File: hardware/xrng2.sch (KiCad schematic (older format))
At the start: 33 parts, among them J101 AVR-PDI-6A, J102 GS3, J103 GS3, J104 Conn_01x02, J105 Conn_01x03, J106 Conn_01x02, J107 USB_B, U101 CD4007, U102 XMEGA64A3U-A, U103 CD4007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

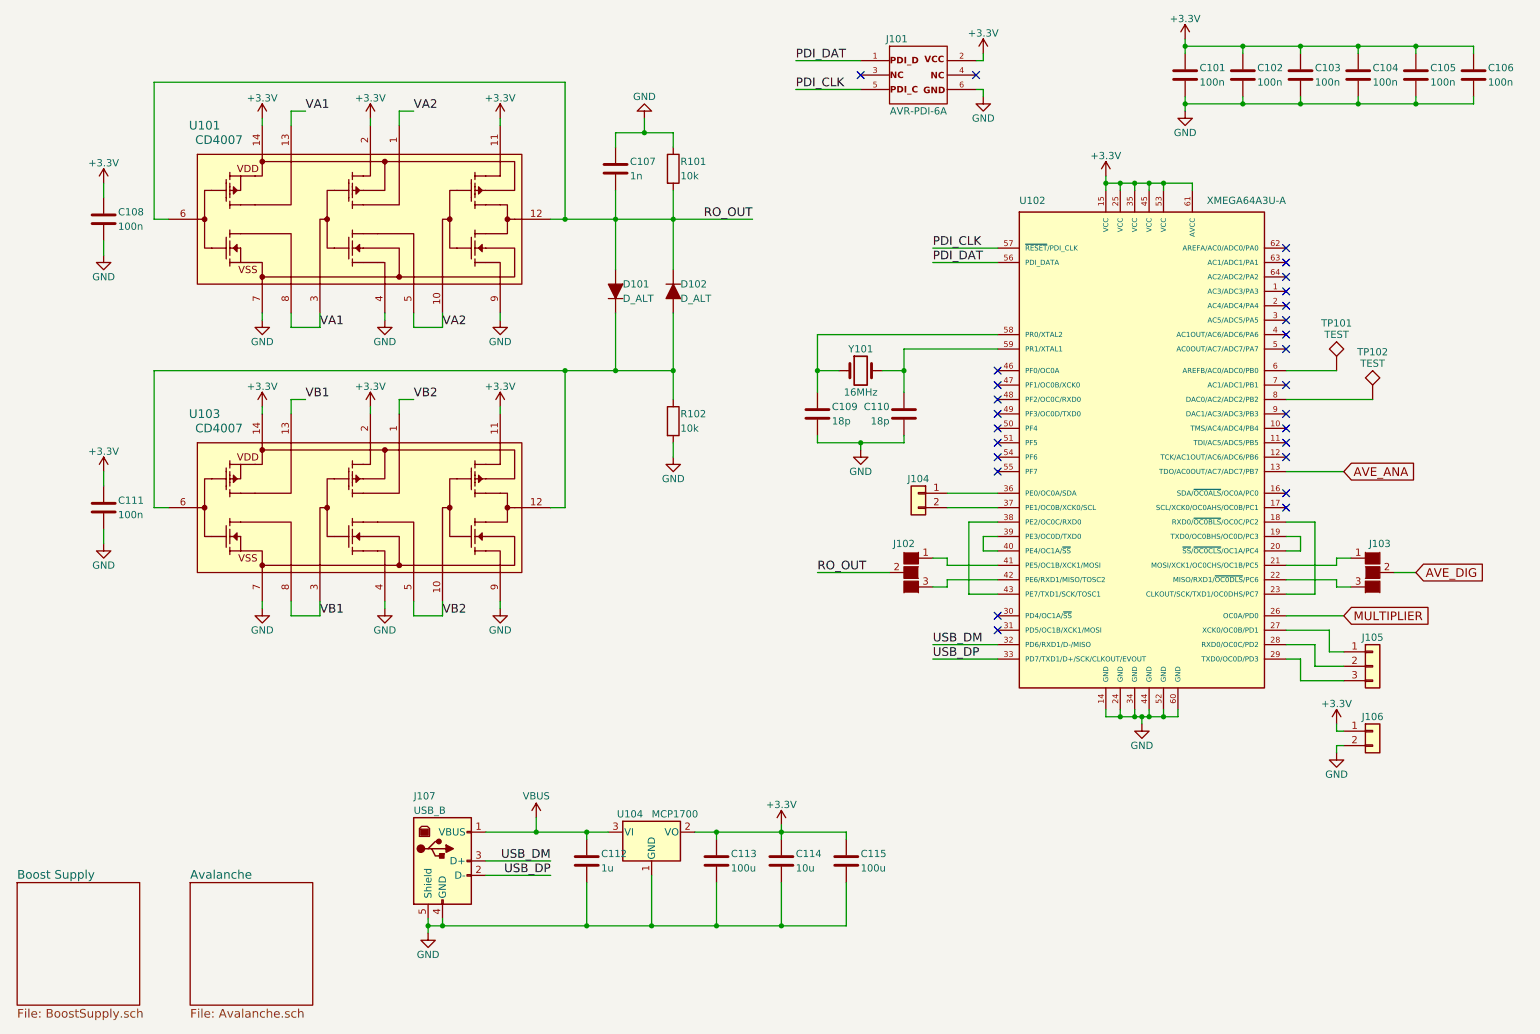
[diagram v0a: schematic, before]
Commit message: Pull-ups for I2C
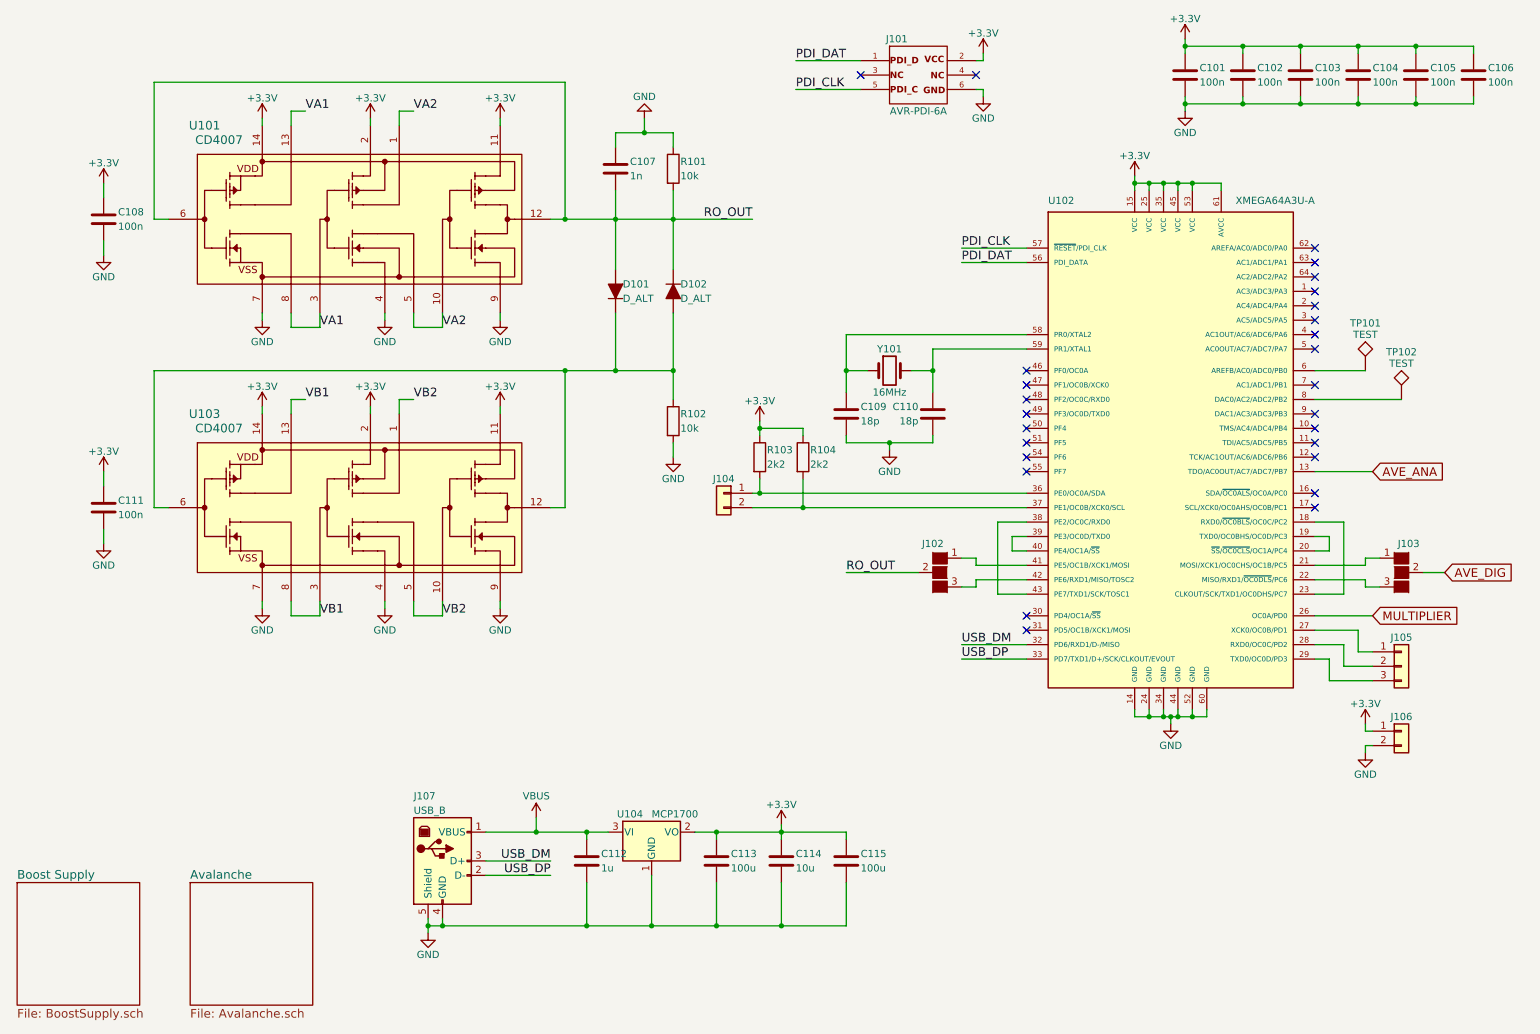
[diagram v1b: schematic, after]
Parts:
- added R103, R104: 2k2, Resistors_SMD:R_0603_HandSoldering, symbol R
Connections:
- net +3V3: now also R103.1, R104.1
- net at J104.1 (Pin_1), U102.36 (PE0/OC0A/SDA): now also R103.2
- net at J104.2 (Pin_2), U102.37 (PE1/OC0B/XCK0/SCL): now also R104.2
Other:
- moved on the sheet: C109, C110, J102, J103, J104, J105, J106, TP101, TP102, U102, Y101

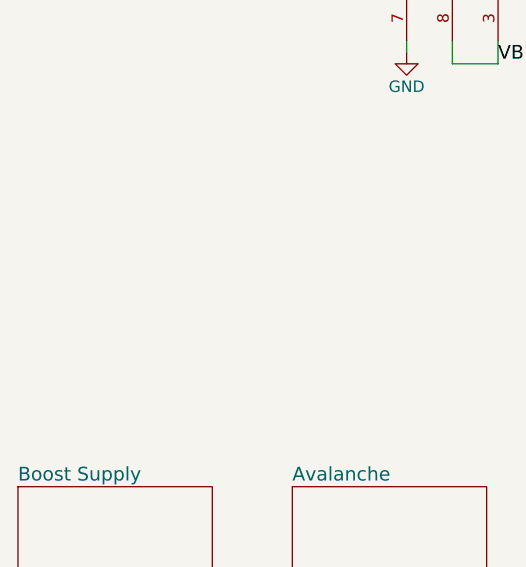
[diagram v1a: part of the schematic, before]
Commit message: Mounting holes
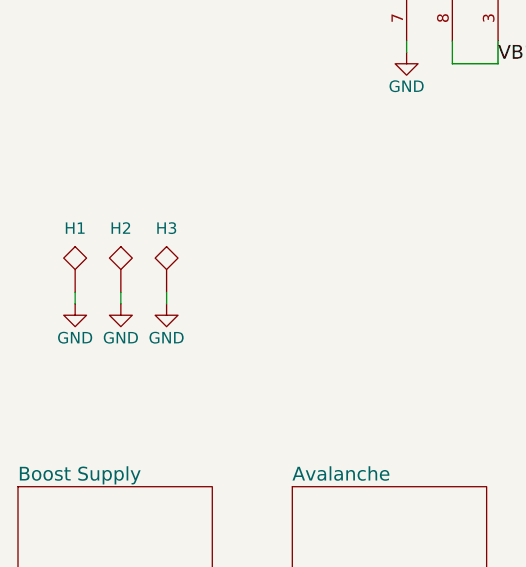
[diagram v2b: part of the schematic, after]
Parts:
- added H1, H2, H3: MOUNT, symbol TEST
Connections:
- net GND: now also H1.1, H2.1, H3.1
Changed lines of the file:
@@
 Connection ~ 6250 3950
 $Comp
-L +3.3V #PWR?
+L +3.3V #PWR031
 U 1 1 5B2942EF
 P 5950 3350
-F 0 "#PWR?" H 5950 3200 50  0001 C CNN
+F 0 "#PWR031" H 5950 3200 50  0001 C CNN
 F 1 "+3.3V" H 5950 3490 50  0000 C CNN
 F 2 "" H 5950 3350 50  0001 C CNN
@@
 	5950 3350 5950 3450
 Connection ~ 5950 3400
+$Comp
+L TEST H1
+U 1 1 5B295B72
+P 1050 5700
+F 0 "H1" H 1050 5950 50  0000 C BNN
+F 1 "MOUNT" H 1050 5950 50  0001 C CNN
+F 2 "" H 1050 5700 50  0001 C CNN
+F 3 "" H 1050 5700 50  0001 C CNN
+	1    1050 5700
+	1    0    0    -1
+$EndComp
+$Comp
+L TEST H2
+U 1 1 5B296169
+P 1250 5700
+F 0 "H2" H 1250 5950 50  0000 C BNN
+F 1 "MOUNT" H 1250 5950 50  0001 C CNN
+F 2 "" H 1250 5700 50  0001 C CNN
+F 3 "" H 1250 5700 50  0001 C CNN
+	1    1250 5700
+	1    0    0    -1
+$EndComp
+$Comp
+L TEST H3
+U 1 1 5B2961EC
+P 1450 5700
+F 0 "H3" H 1450 5950 50  0000 C BNN
+F 1 "MOUNT" H 1450 5950 50  0001 C CNN
+F 2 "" H 1450 5700 50  0001 C CNN
+F 3 "" H 1450 5700 50  0001 C CNN
+	1    1450 5700
+	1    0    0    -1
+$EndComp
+$Comp
+L GND #PWR?
+U 1 1 5B296314
+P 1050 5750
+F 0 "#PWR?" H 1050 5500 50  0001 C CNN
+F 1 "GND" H 1050 5600 50  0000 C CNN
+F 2 "" H 1050 5750 50  0001 C CNN
+F 3 "" H 1050 5750 50  0001 C CNN
+	1    1050 5750
+	1    0    0    -1
+$EndComp
+$Comp
+L GND #PWR?
+U 1 1 5B296391
+P 1250 5750
+F 0 "#PWR?" H 1250 5500 50  0001 C CNN
+F 1 "GND" H 1250 5600 50  0000 C CNN
+F 2 "" H 1250 5750 50  0001 C CNN
+F 3 "" H 1250 5750 50  0001 C CNN
+	1    1250 5750
+	1    0    0    -1
+$EndComp
+$Comp
+L GND #PWR?
+U 1 1 5B29640E
+P 1450 5750
+F 0 "#PWR?" H 1450 5500 50  0001 C CNN
+F 1 "GND" H 1450 5600 50  0000 C CNN
+F 2 "" H 1450 5750 50  0001 C CNN
+F 3 "" H 1450 5750 50  0001 C CNN
+	1    1450 5750
+	1    0    0    -1
+$EndComp
+Wire Wire Line
+	1450 5750 1450 5700
+Wire Wire Line
+	1250 5700 1250 5750
+Wire Wire Line
+	1050 5750 1050 5700
 $EndSCHEMATC

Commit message: Mounting holes
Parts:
- H1, H2, H3: footprint (none) -> Mounting_Holes:MountingHole_3.2mm_M3
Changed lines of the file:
@@
 F 0 "H1" H 1050 5950 50  0000 C BNN
 F 1 "MOUNT" H 1050 5950 50  0001 C CNN
-F 2 "" H 1050 5700 50  0001 C CNN
+F 2 "Mounting_Holes:MountingHole_3.2mm_M3" H 1050 5700 50  0001 C CNN
 F 3 "" H 1050 5700 50  0001 C CNN
 	1    1050 5700
@@
 F 0 "H2" H 1250 5950 50  0000 C BNN
 F 1 "MOUNT" H 1250 5950 50  0001 C CNN
-F 2 "" H 1250 5700 50  0001 C CNN
+F 2 "Mounting_Holes:MountingHole_3.2mm_M3" H 1250 5700 50  0001 C CNN
 F 3 "" H 1250 5700 50  0001 C CNN
 	1    1250 5700
@@
 F 0 "H3" H 1450 5950 50  0000 C BNN
 F 1 "MOUNT" H 1450 5950 50  0001 C CNN
-F 2 "" H 1450 5700 50  0001 C CNN
+F 2 "Mounting_Holes:MountingHole_3.2mm_M3" H 1450 5700 50  0001 C CNN
 F 3 "" H 1450 5700 50  0001 C CNN
 	1    1450 5700
@@
 $EndComp
 $Comp
-L GND #PWR?
+L GND #PWR032
 U 1 1 5B296314
 P 1050 5750
-F 0 "#PWR?" H 1050 5500 50  0001 C CNN
+F 0 "#PWR032" H 1050 5500 50  0001 C CNN
 F 1 "GND" H 1050 5600 50  0000 C CNN
 F 2 "" H 1050 5750 50  0001 C CNN
@@
 $EndComp
 $Comp
-L GND #PWR?
+L GND #PWR033
 U 1 1 5B296391
 P 1250 5750
-F 0 "#PWR?" H 1250 5500 50  0001 C CNN
+F 0 "#PWR033" H 1250 5500 50  0001 C CNN
 F 1 "GND" H 1250 5600 50  0000 C CNN
 F 2 "" H 1250 5750 50  0001 C CNN
@@
 $EndComp
 $Comp
-L GND #PWR?
+L GND #PWR034
 U 1 1 5B29640E
 P 1450 5750
-F 0 "#PWR?" H 1450 5500 50  0001 C CNN
+F 0 "#PWR034" H 1450 5500 50  0001 C CNN
 F 1 "GND" H 1450 5600 50  0000 C CNN
 F 2 "" H 1450 5750 50  0001 C CNN

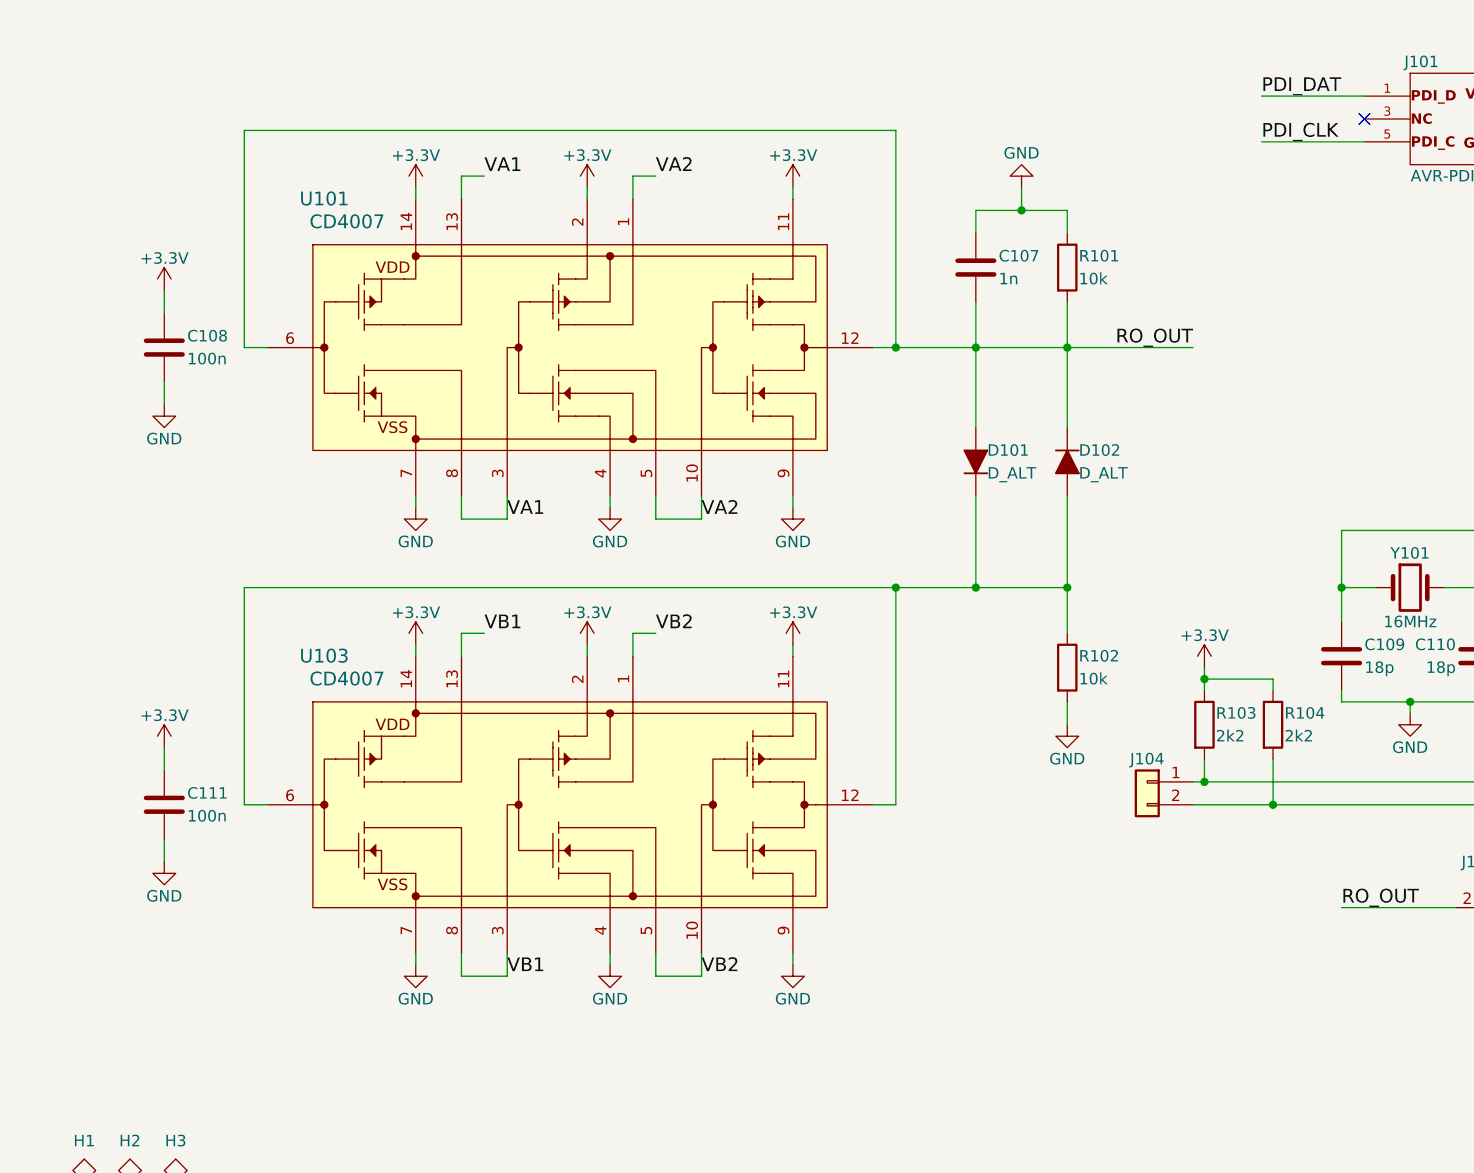
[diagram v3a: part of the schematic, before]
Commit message: XOR mixer
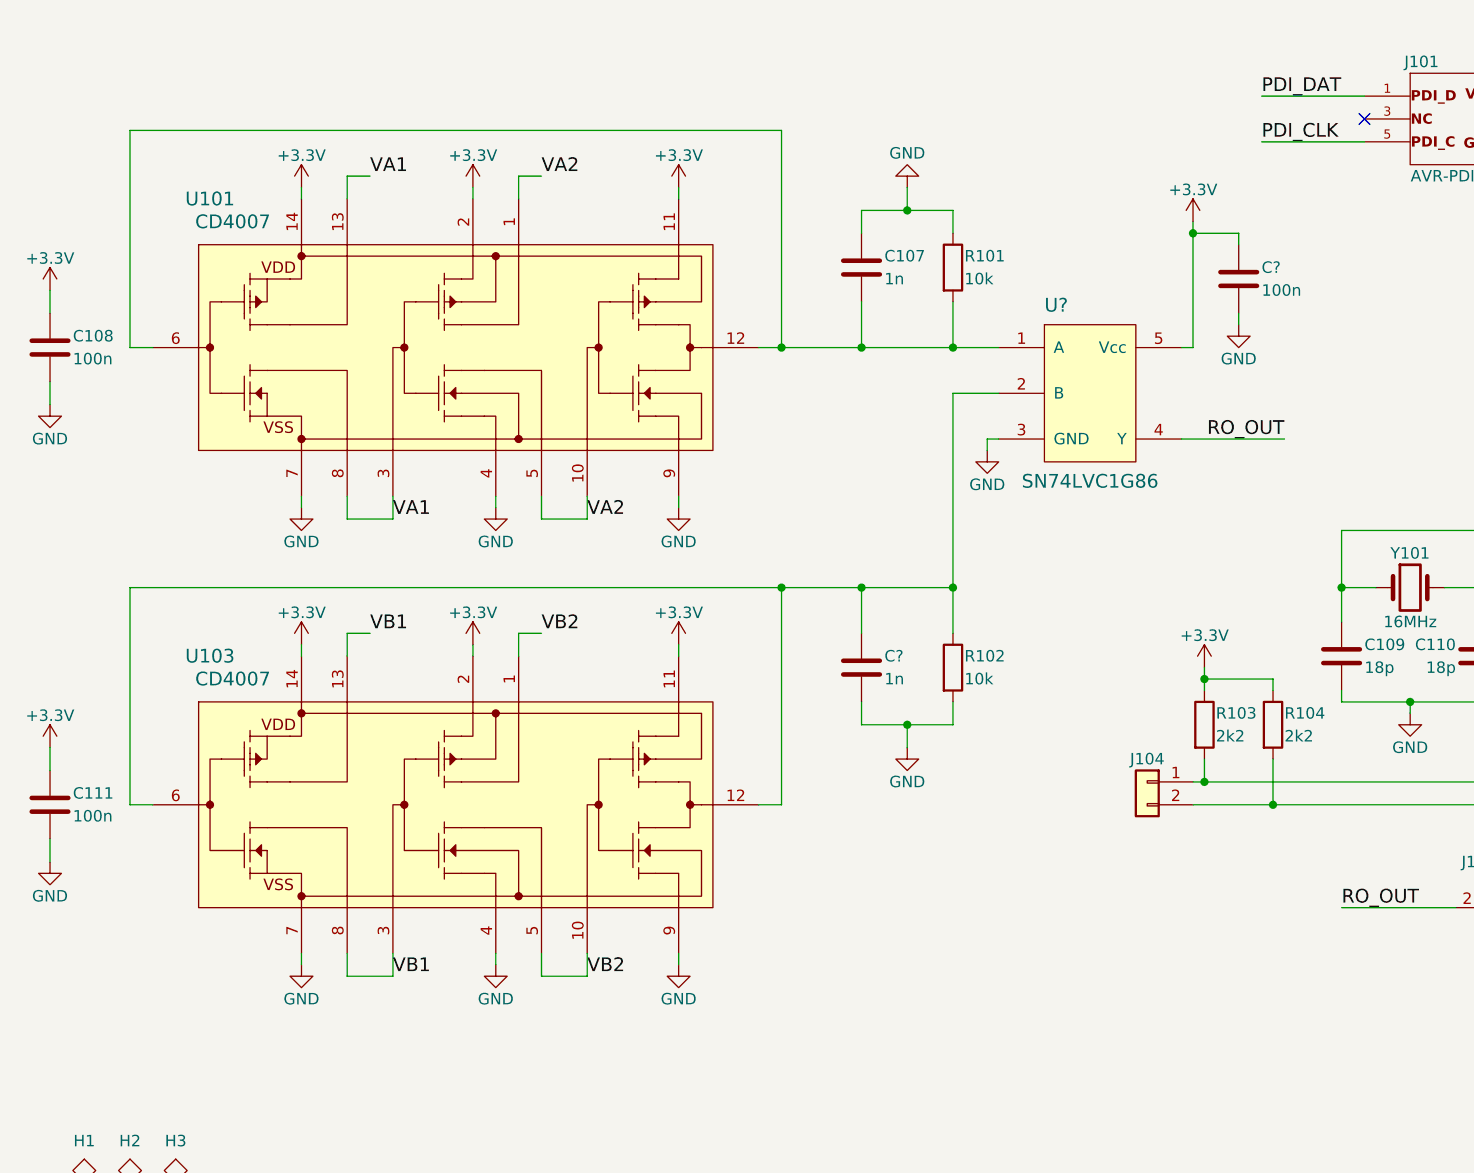
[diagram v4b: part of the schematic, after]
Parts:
- removed D101, D102: D_ALT, Diodes_SMD:D_SOD-523, symbol D_ALT
- added C?: 100n, Capacitors_SMD:C_0603_HandSoldering, symbol C
- added C?: 1n, Capacitors_SMD:C_0603_HandSoldering, symbol C
- added U?: SN74LVC1G86, symbol SN74LVC1G86
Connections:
- net +3V3: now also C?.1, U?.5 (Vcc)
- net GND: now also C?.2, C?.2, U?.3 (GND)
- net RO_OUT: now also U?.4 (Y); no longer C107.2, R101.2, U101.12 (3Y), U101.6 (1A)
- net at R102.1, U103.12 (3Y), U103.6 (1A): now also C?.1, U?.2 (B)
- new net: C107.2, R101.2, U101.12 (3Y), U101.6 (1A), U?.1 (A)
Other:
- moved on the sheet: C107, C108, C111, R101, R102, U101, U103

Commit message: DRC
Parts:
- gave numbers to parts that had none: 3
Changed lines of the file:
@@
 	1050 5750 1050 5700
 $Comp
-L SN74LVC1G86 U?
+L SN74LVC1G86 U105
 U 1 1 5B2B78B0
 P 5450 2150
-F 0 "U?" H 5250 2500 60  0000 L BNN
+F 0 "U105" H 5250 2500 60  0000 L BNN
 F 1 "SN74LVC1G86" H 5450 1800 60  0000 C TNN
 F 2 "" H 5450 2150 60  0001 C CNN
@@
 	4850 2150 5050 2150
 $Comp
-L GND #PWR?
+L GND #PWR035
 U 1 1 5B2B863F
 P 5000 2400
-F 0 "#PWR?" H 5000 2150 50  0001 C CNN
+F 0 "#PWR035" H 5000 2150 50  0001 C CNN
 F 1 "GND" H 5000 2250 50  0000 C CNN
 F 2 "" H 5000 2400 50  0001 C CNN
@@
 	5000 2350 5000 2400
 $Comp
-L +3.3V #PWR?
+L +3.3V #PWR036
 U 1 1 5B2B8A85
 P 5900 1400
-F 0 "#PWR?" H 5900 1250 50  0001 C CNN
+F 0 "#PWR036" H 5900 1250 50  0001 C CNN
 F 1 "+3.3V" H 5900 1540 50  0000 C CNN
 F 2 "" H 5900 1400 50  0001 C CNN
@@
 $EndComp
 $Comp
-L C C?
+L C C116
 U 1 1 5B2B9064
 P 6100 1650
-F 0 "C?" H 6200 1700 50  0000 L CNN
+F 0 "C116" H 6200 1700 50  0000 L CNN
 F 1 "100n" H 6200 1600 50  0000 L CNN
 F 2 "Capacitors_SMD:C_0603_HandSoldering" H 6138 1500 50  0001 C CNN
@@
 Connection ~ 5900 1450
 $Comp
-L GND #PWR?
+L GND #PWR037
 U 1 1 5B2B95FF
 P 6100 1850
-F 0 "#PWR?" H 6100 1600 50  0001 C CNN
+F 0 "#PWR037" H 6100 1600 50  0001 C CNN
 F 1 "GND" H 6100 1700 50  0000 C CNN
 F 2 "" H 6100 1850 50  0001 C CNN
@@
 	6100 1850 6100 1800
 $Comp
-L C C?
+L C C117
 U 1 1 5B2BA018
 P 4450 3350
-F 0 "C?" H 4550 3400 50  0000 L CNN
+F 0 "C117" H 4550 3400 50  0000 L CNN
 F 1 "1n" H 4550 3300 50  0000 L CNN
 F 2 "Capacitors_SMD:C_0603_HandSoldering" H 4488 3200 50  0001 C CNN

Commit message: Footprint
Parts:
- U105: footprint (none) -> TO_SOT_Packages_SMD:SOT-23-5
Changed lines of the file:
@@
 F 0 "U105" H 5250 2500 60  0000 L BNN
 F 1 "SN74LVC1G86" H 5450 1800 60  0000 C TNN
-F 2 "" H 5450 2150 60  0001 C CNN
+F 2 "TO_SOT_Packages_SMD:SOT-23-5" H 5450 2150 60  0001 C CNN
 F 3 "" H 5450 2150 60  0001 C CNN
 	1    5450 2150
